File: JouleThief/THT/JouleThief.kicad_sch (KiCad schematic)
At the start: 14 parts, among them J1 Screw_Terminal_01x02, J2 Screw_Terminal_01x02, Q1 BC547, Q2 BC547

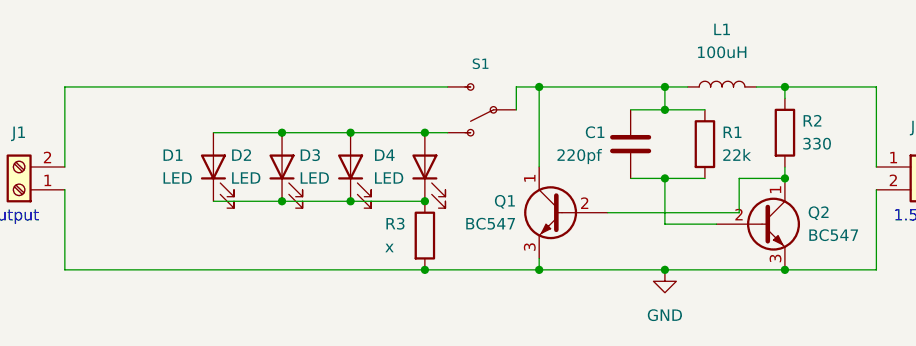
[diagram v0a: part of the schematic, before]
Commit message: Updated Joule thief schematic values
Inductor: 220uH
Capacitor: 100pF
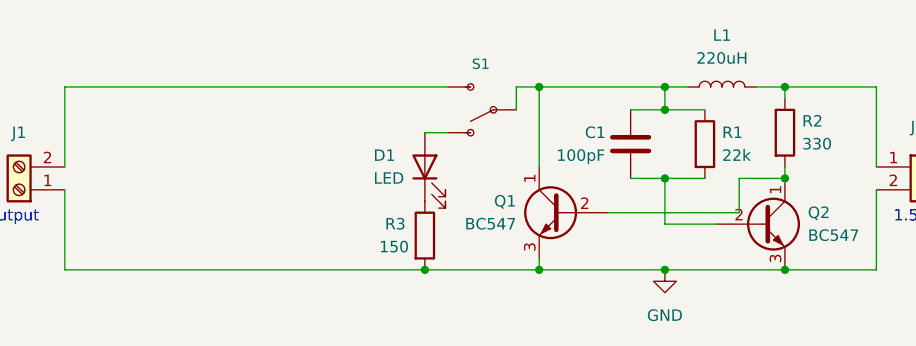
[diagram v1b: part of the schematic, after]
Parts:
- removed D1, D2, D3: LED, LED_SMD:LED_0805_2012Metric_Pad1.15x1.40mm_HandSolder, symbol Device:LED
- C1: value 220pf -> 100pF
- L1: value 100uH -> 220uH
- R3: value x -> 150
- renumbered D4 to D1
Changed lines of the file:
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@@
   (junction (at 151.765 90.805) (diameter 0) (color 0 0 0 0)
   )
-  (junction (at 109.22 95.885) (diameter 0) (color 0 0 0 0)
-  )
   (junction (at 137.795 90.805) (diameter 0) (color 0 0 0 0)
   )
   (junction (at 151.765 100.965) (diameter 0) (color 0 0 0 0)
   )
-  (junction (at 109.22 103.505) (diameter 0) (color 0 0 0 0)
-  )
   (junction (at 165.1 100.965) (diameter 0) (color 0 0 0 0)
   )
-  (junction (at 116.84 103.505) (diameter 0) (color 0 0 0 0)
-  )
   (junction (at 151.765 111.125) (diameter 0) (color 0 0 0 0)
   )
-  (junction (at 125.095 95.885) (diameter 0) (color 0 0 0 0)
-  )
-  (junction (at 116.84 95.885) (diameter 0) (color 0 0 0 0)
-  )
   (junction (at 125.095 111.125) (diameter 0) (color 0 0 0 0)
   )
@@
   (junction (at 165.1 111.125) (diameter 0) (color 0 0 0 0)
   )
-  (junction (at 125.095 103.505) (diameter 0) (color 0 0 0 0)
-  )
   (junction (at 165.1 90.805) (diameter 0) (color 0 0 0 0)
   )
@@
     (stroke (width 0) (type default) (color 0 0 0 0))
   )
-  (wire (pts (xy 109.22 103.505) (xy 116.84 103.505))
-    (stroke (width 0) (type default) (color 0 0 0 0))
-  )
   (wire (pts (xy 137.795 109.855) (xy 137.795 111.125))
     (stroke (width 0) (type default) (color 0 0 0 0))
   )
-  (wire (pts (xy 116.84 103.505) (xy 125.095 103.505))
-    (stroke (width 0) (type default) (color 0 0 0 0))
-  )
   (wire (pts (xy 147.955 100.965) (xy 151.765 100.965))
     (stroke (width 0) (type default) (color 0 0 0 0))
@@
     (stroke (width 0) (type default) (color 0 0 0 0))
   )
-  (wire (pts (xy 116.84 95.885) (xy 125.095 95.885))
-    (stroke (width 0) (type default) (color 0 0 0 0))
-  )
   (wire (pts (xy 156.21 93.345) (xy 151.765 93.345))
     (stroke (width 0) (type default) (color 0 0 0 0))
@@
     (stroke (width 0) (type default) (color 0 0 0 0))
   )
-  (wire (pts (xy 101.6 103.505) (xy 109.22 103.505))
-    (stroke (width 0) (type default) (color 0 0 0 0))
-  )
   (wire (pts (xy 151.765 100.965) (xy 156.21 100.965))
     (stroke (width 0) (type default) (color 0 0 0 0))
@@
     (stroke (width 0) (type default) (color 0 0 0 0))
   )
-  (wire (pts (xy 101.6 95.885) (xy 109.22 95.885))
-    (stroke (width 0) (type default) (color 0 0 0 0))
-  )
   (wire (pts (xy 175.26 90.805) (xy 165.1 90.805))
     (stroke (width 0) (type default) (color 0 0 0 0))
@@
   )
   (wire (pts (xy 135.255 93.345) (xy 135.255 90.805))
-    (stroke (width 0) (type default) (color 0 0 0 0))
-  )
-  (wire (pts (xy 109.22 95.885) (xy 116.84 95.885))
     (stroke (width 0) (type default) (color 0 0 0 0))
   )
@@
     (pin "2")
   )
-  (symbol (lib_id "Device:LED") (at 116.84 99.695 90) (unit 1)
-    (in_bom yes) (on_board yes)
-    (property "Reference" "D3" (id 0) (at 111.125 98.425 90)
-      (effects (font (size 1.27 1.27)) (justify right))
-    )
-    (property "Value" "LED" (id 1) (at 111.125 100.965 90)
-      (effects (font (size 1.27 1.27)) (justify right))
-    )
-    (property "Footprint" "LED_SMD:LED_0805_2012Metric_Pad1.15x1.40mm_HandSolder" (id 2) (at 116.84 99.695 0)
-      (effects (font (size 1.27 1.27)) hide)
-    )
-    (property "Datasheet" "~" (id 3) (at 116.84 99.695 0)
-      (effects (font (size 1.27 1.27)) hide)
-    )
-    (pin "1")
-    (pin "2")
-  )
   (symbol (lib_id "Device:L") (at 158.115 90.805 90) (unit 1)
     (in_bom yes) (on_board yes) (fields_autoplaced)
-    (property "Reference" "L1" (id 0) (at 158.115 84.455 90))
-    (property "Value" "100uH" (id 1) (at 158.115 86.995 90))
+    (property "Reference" "L1" (id 0) (at 158.115 85.09 90))
+    (property "Value" "220uH" (id 1) (at 158.115 87.63 90))
     (property "Footprint" "Inductor_SMD:L_6.3x6.3_H3" (id 2) (at 158.115 90.805 0)
       (effects (font (size 1.27 1.27)) hide)
@@
       (effects (font (size 1.27 1.27)) (justify left))
     )
-    (property "Value" "220pf" (id 1) (at 139.7 98.425 0)
+    (property "Value" "100pF" (id 1) (at 139.7 98.425 0)
       (effects (font (size 1.27 1.27)) (justify left))
     )
@@
     (pin "1")
   )
-  (symbol (lib_id "Device:LED") (at 101.6 99.695 90) (unit 1)
-    (in_bom yes) (on_board yes)
-    (property "Reference" "D1" (id 0) (at 95.885 98.425 90)
-      (effects (font (size 1.27 1.27)) (justify right))
-    )
-    (property "Value" "LED" (id 1) (at 95.885 100.965 90)
-      (effects (font (size 1.27 1.27)) (justify right))
-    )
-    (property "Footprint" "LED_SMD:LED_0805_2012Metric_Pad1.15x1.40mm_HandSolder" (id 2) (at 101.6 99.695 0)
-      (effects (font (size 1.27 1.27)) hide)
-    )
-    (property "Datasheet" "~" (id 3) (at 101.6 99.695 0)
-      (effects (font (size 1.27 1.27)) hide)
-    )
-    (pin "1")
-    (pin "2")
-  )
   (symbol (lib_id "Connector:Screw_Terminal_01x02") (at 80.01 102.235 180) (unit 1)
     (in_bom yes) (on_board yes) (fields_autoplaced)
@@
     (pin "2")
   )
-  (symbol (lib_id "Device:LED") (at 109.22 99.695 90) (unit 1)
-    (in_bom yes) (on_board yes)
-    (property "Reference" "D2" (id 0) (at 103.505 98.425 90)
-      (effects (font (size 1.27 1.27)) (justify right))
-    )
-    (property "Value" "LED" (id 1) (at 103.505 100.965 90)
-      (effects (font (size 1.27 1.27)) (justify right))
-    )
-    (property "Footprint" "LED_SMD:LED_0805_2012Metric_Pad1.15x1.40mm_HandSolder" (id 2) (at 109.22 99.695 0)
-      (effects (font (size 1.27 1.27)) hide)
-    )
-    (property "Datasheet" "~" (id 3) (at 109.22 99.695 0)
-      (effects (font (size 1.27 1.27)) hide)
-    )
-    (pin "1")
-    (pin "2")
-  )
   (symbol (lib_id "Device:R") (at 156.21 97.155 0) (unit 1)
     (in_bom yes) (on_board yes)
@@
   (symbol (lib_id "Device:LED") (at 125.095 99.695 90) (unit 1)
     (in_bom yes) (on_board yes)
-    (property "Reference" "D4" (id 0) (at 119.38 98.425 90)
+    (property "Reference" "D1" (id 0) (at 119.38 98.425 90)
       (effects (font (size 1.27 1.27)) (justify right))
     )
@@
       (effects (font (size 1.27 1.27)) (justify left))
     )
-    (property "Value" "x" (id 1) (at 120.65 108.585 0)
+    (property "Value" "150" (id 1) (at 120.015 108.585 0)
       (effects (font (size 1.27 1.27)) (justify left))
     )
@@
     )
     (path "/56f57a0c-d952-4b14-b499-4833f5f6a321"
-      (reference "C1") (unit 1) (value "220pf") (footprint "Capacitor_SMD:C_0805_2012Metric_Pad1.18x1.45mm_HandSolder")
-    )
-    (path "/a3379bb9-2fa5-4298-a436-0e0faa7bcb5e"
+      (reference "C1") (unit 1) (value "100pF") (footprint "Capacitor_SMD:C_0805_2012Metric_Pad1.18x1.45mm_HandSolder")
+    )
+    (path "/e027e40e-245b-4b6b-928b-0501a7da5de5"
       (reference "D1") (unit 1) (value "LED") (footprint "LED_SMD:LED_0805_2012Metric_Pad1.15x1.40mm_HandSolder")
-    )
-    (path "/d156950b-aa7e-4415-90f6-d17a4996de0e"
-      (reference "D2") (unit 1) (value "LED") (footprint "LED_SMD:LED_0805_2012Metric_Pad1.15x1.40mm_HandSolder")
-    )
-    (path "/2c5e3b91-00a4-441c-a5d0-5cef8c01ab08"
-      (reference "D3") (unit 1) (value "LED") (footprint "LED_SMD:LED_0805_2012Metric_Pad1.15x1.40mm_HandSolder")
-    )
-    (path "/e027e40e-245b-4b6b-928b-0501a7da5de5"
-      (reference "D4") (unit 1) (value "LED") (footprint "LED_SMD:LED_0805_2012Metric_Pad1.15x1.40mm_HandSolder")
     )
     (path "/c5208d8c-5be5-4514-b93e-909a9ac14ee6"
@@
     )
     (path "/41c982a7-98bb-4b69-93c8-cae707855073"
-      (reference "L1") (unit 1) (value "100uH") (footprint "Inductor_SMD:L_6.3x6.3_H3")
+      (reference "L1") (unit 1) (value "220uH") (footprint "Inductor_SMD:L_6.3x6.3_H3")
     )
     (path "/473a4415-2386-4149-a3fe-7889d826e6e0"
@@
     )
     (path "/fec27d13-0747-41e3-a4d8-e21a45052ada"
-      (reference "R3") (unit 1) (value "x") (footprint "Resistor_SMD:R_0805_2012Metric_Pad1.20x1.40mm_HandSolder")
+      (reference "R3") (unit 1) (value "150") (footprint "Resistor_SMD:R_0805_2012Metric_Pad1.20x1.40mm_HandSolder")
     )
     (path "/5a60103d-c1f5-44fb-9ca6-bd09329bef56"

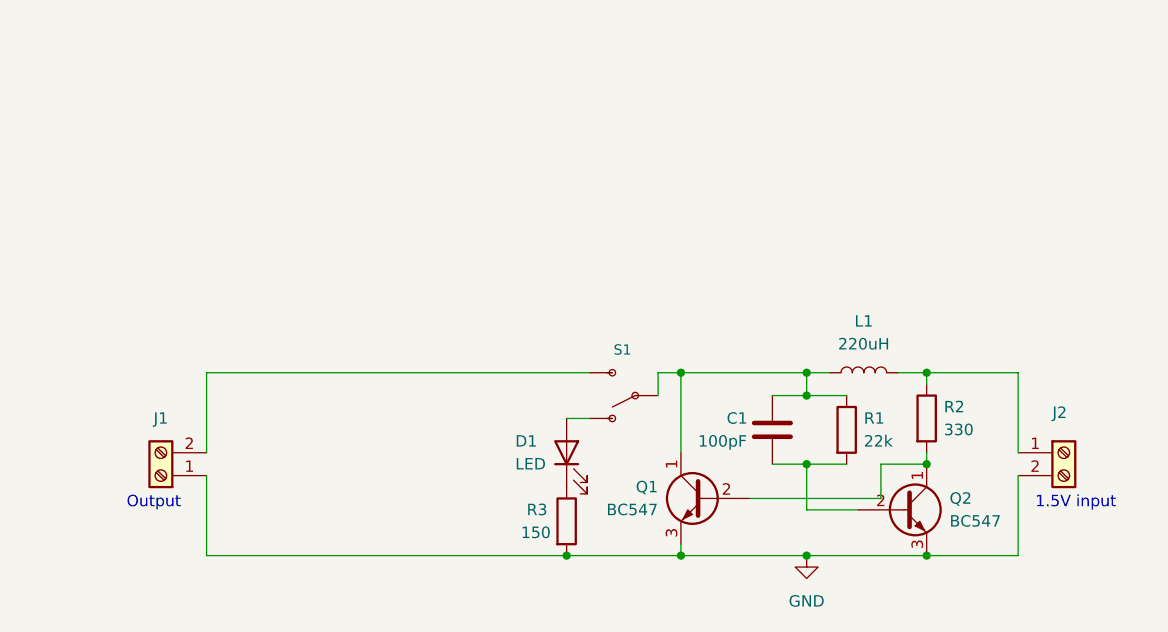
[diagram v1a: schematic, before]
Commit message: added tht components back tot tht
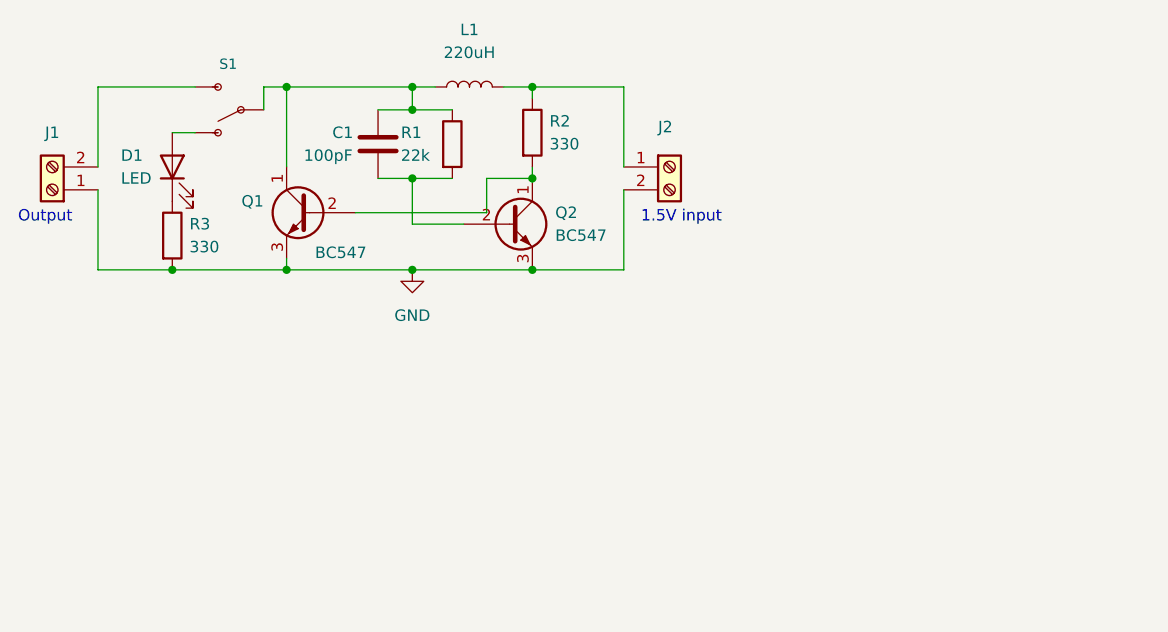
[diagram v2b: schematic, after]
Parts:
- C1: footprint Capacitor_SMD:C_0805_2012Metric_Pad1.18x1.45mm_HandSolder -> Capacitor_THT:C_Axial_L5.1mm_D3.1mm_P7.50mm_Horizontal
- D1: footprint LED_SMD:LED_0805_2012Metric_Pad1.15x1.40mm_HandSolder -> LED_THT:LED_D5.0mm_Clear
- L1: footprint Inductor_SMD:L_6.3x6.3_H3 -> Inductor_THT:L_Axial_L5.0mm_D3.6mm_P10.00mm_Horizontal_Murata_BL01RN1A2A2
- Q1, Q2: footprint SamacSys_Parts:BC847215 -> Package_TO_SOT_THT:TO-92_Inline
- R1, R2: footprint Resistor_SMD:R_0805_2012Metric_Pad1.20x1.40mm_HandSolder -> Resistor_THT:R_Axial_DIN0204_L3.6mm_D1.6mm_P7.62mm_Horizontal
- R3: value 150 -> 330; footprint Resistor_SMD:R_0805_2012Metric_Pad1.20x1.40mm_HandSolder -> Resistor_THT:R_Axial_DIN0204_L3.6mm_D1.6mm_P7.62mm_Horizontal; Purpose led current resistor -> (none)
- S1: footprint SamacSys_Parts:LSSM12PVTR -> SnapEDA Library:SW_1825159-1

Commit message: enh
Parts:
- C1: footprint Capacitor_THT:C_Axial_L5.1mm_D3.1mm_P7.50mm_Horizontal -> Capacitor_SMD:C_0805_2012Metric_Pad1.18x1.45mm_HandSolder
- D1: footprint LED_THT:LED_D5.0mm_Clear -> LED_SMD:LED_0805_2012Metric_Pad1.15x1.40mm_HandSolder
- L1: footprint Inductor_THT:L_Axial_L5.0mm_D3.6mm_P10.00mm_Horizontal_Murata_BL01RN1A2A2 -> Inductor_SMD:L_6.3x6.3_H3
- Q1, Q2: footprint Package_TO_SOT_THT:TO-92_Inline -> SamacSys_Parts:BC847215
- R1, R2, R3: footprint Resistor_THT:R_Axial_DIN0204_L3.6mm_D1.6mm_P7.62mm_Horizontal -> Resistor_SMD:R_0805_2012Metric_Pad1.20x1.40mm_HandSolder
- S1: footprint SnapEDA Library:SW_1825159-1 -> SamacSys_Parts:LSSM12PVTR
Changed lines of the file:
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@@
       (effects (font (size 1.27 1.27)) (justify left))
     )
-    (property "Footprint" "Capacitor_THT:C_Axial_L5.1mm_D3.1mm_P7.50mm_Horizontal" (id 2) (at 105.1052 69.215 0)
+    (property "Footprint" "Capacitor_SMD:C_0805_2012Metric_Pad1.18x1.45mm_HandSolder" (id 2) (at 105.1052 69.215 0)
       (effects (font (size 1.27 1.27)) hide)
     )
@@
     (property "Reference" "L1" (id 0) (at 114.3 52.705 90))
     (property "Value" "220uH" (id 1) (at 114.3 55.245 90))
-    (property "Footprint" "Inductor_THT:L_Axial_L5.0mm_D3.6mm_P10.00mm_Horizontal_Murata_BL01RN1A2A2" (id 2) (at 114.3 59.055 0)
+    (property "Footprint" "Inductor_SMD:L_6.3x6.3_H3" (id 2) (at 114.3 59.055 0)
       (effects (font (size 1.27 1.27)) hide)
     )
@@
       (effects (font (size 1.27 1.27)) (justify left))
     )
-    (property "Footprint" "Package_TO_SOT_THT:TO-92_Inline" (id 2) (at 123.825 76.2 0)
+    (property "Footprint" "SamacSys_Parts:BC847215" (id 2) (at 123.825 76.2 0)
       (effects (font (size 1.27 1.27) italic) (justify left) hide)
     )
@@
       (effects (font (size 1.27 1.27)) (justify left))
     )
-    (property "Footprint" "Resistor_THT:R_Axial_DIN0204_L3.6mm_D1.6mm_P7.62mm_Horizontal" (id 2) (at 110.617 65.405 90)
+    (property "Footprint" "Resistor_SMD:R_0805_2012Metric_Pad1.20x1.40mm_HandSolder" (id 2) (at 110.617 65.405 90)
       (effects (font (size 1.27 1.27)) hide)
     )
@@
       (effects (font (size 1.27 1.27)) (justify left))
     )
-    (property "Footprint" "Resistor_THT:R_Axial_DIN0204_L3.6mm_D1.6mm_P7.62mm_Horizontal" (id 2) (at 119.507 64.135 90)
+    (property "Footprint" "Resistor_SMD:R_0805_2012Metric_Pad1.20x1.40mm_HandSolder" (id 2) (at 119.507 64.135 90)
       (effects (font (size 1.27 1.27)) hide)
     )
@@
       (effects (font (size 1.27 1.27)) (justify right))
     )
-    (property "Footprint" "LED_THT:LED_D5.0mm_Clear" (id 2) (at 81.28 67.945 0)
+    (property "Footprint" "LED_SMD:LED_0805_2012Metric_Pad1.15x1.40mm_HandSolder" (id 2) (at 81.28 67.945 0)
       (effects (font (size 1.27 1.27)) hide)
     )
@@
       (effects (font (size 1.27 1.27)) (justify left))
     )
-    (property "Footprint" "Resistor_THT:R_Axial_DIN0204_L3.6mm_D1.6mm_P7.62mm_Horizontal" (id 2) (at 79.502 75.565 90)
+    (property "Footprint" "Resistor_SMD:R_0805_2012Metric_Pad1.20x1.40mm_HandSolder" (id 2) (at 79.502 75.565 90)
       (effects (font (size 1.27 1.27)) hide)
     )
@@
       (effects (font (size 1.143 1.143)) hide)
     )
-    (property "Footprint" "SnapEDA Library:SW_1825159-1" (id 2) (at 88.9 67.945 0)
+    (property "Footprint" "SamacSys_Parts:LSSM12PVTR" (id 2) (at 88.9 67.945 0)
       (effects (font (size 0.508 0.508)) hide)
     )
@@
       (effects (font (size 1.27 1.27)) (justify left))
     )
-    (property "Footprint" "Package_TO_SOT_THT:TO-92_Inline" (id 2) (at 91.44 74.93 0)
+    (property "Footprint" "SamacSys_Parts:BC847215" (id 2) (at 91.44 74.93 0)
       (effects (font (size 1.27 1.27) italic) (justify left) hide)
     )
@@
     )
     (path "/165ce1d9-ec6c-402f-b137-29c897fe33e9"
-      (reference "C1") (unit 1) (value "100pF") (footprint "Capacitor_THT:C_Axial_L5.1mm_D3.1mm_P7.50mm_Horizontal")
+      (reference "C1") (unit 1) (value "100pF") (footprint "Capacitor_SMD:C_0805_2012Metric_Pad1.18x1.45mm_HandSolder")
     )
     (path "/7e6f3694-d55b-4625-b9f4-5a2ce49e4fea"
-      (reference "D1") (unit 1) (value "LED") (footprint "LED_THT:LED_D5.0mm_Clear")
+      (reference "D1") (unit 1) (value "LED") (footprint "LED_SMD:LED_0805_2012Metric_Pad1.15x1.40mm_HandSolder")
     )
     (path "/2987da22-2eec-4ed1-b4c8-42061a16b495"
@@
     )
     (path "/3d2a249b-2f29-4cd7-a76b-1d51a3ee2fab"
-      (reference "L1") (unit 1) (value "220uH") (footprint "Inductor_THT:L_Axial_L5.0mm_D3.6mm_P10.00mm_Horizontal_Murata_BL01RN1A2A2")
+      (reference "L1") (unit 1) (value "220uH") (footprint "Inductor_SMD:L_6.3x6.3_H3")
     )
     (path "/fbe24f0e-fbe5-41ce-aecf-066aa14fabc3"
-      (reference "Q1") (unit 1) (value "BC547") (footprint "Package_TO_SOT_THT:TO-92_Inline")
+      (reference "Q1") (unit 1) (value "BC547") (footprint "SamacSys_Parts:BC847215")
     )
     (path "/56f97ceb-2f89-45b9-8233-472a8c58f4ba"
-      (reference "Q2") (unit 1) (value "BC547") (footprint "Package_TO_SOT_THT:TO-92_Inline")
+      (reference "Q2") (unit 1) (value "BC547") (footprint "SamacSys_Parts:BC847215")
     )
     (path "/599fa2b0-cb4d-4f48-a63f-0382fedb8334"
-      (reference "R1") (unit 1) (value "22k") (footprint "Resistor_THT:R_Axial_DIN0204_L3.6mm_D1.6mm_P7.62mm_Horizontal")
+      (reference "R1") (unit 1) (value "22k") (footprint "Resistor_SMD:R_0805_2012Metric_Pad1.20x1.40mm_HandSolder")
     )
     (path "/5b4da779-33b4-456c-8ed4-c656d4dde8be"
-      (reference "R2") (unit 1) (value "330") (footprint "Resistor_THT:R_Axial_DIN0204_L3.6mm_D1.6mm_P7.62mm_Horizontal")
+      (reference "R2") (unit 1) (value "330") (footprint "Resistor_SMD:R_0805_2012Metric_Pad1.20x1.40mm_HandSolder")
     )
     (path "/9d64a416-99e7-4e05-b7be-bdba073d7f38"
-      (reference "R3") (unit 1) (value "330") (footprint "Resistor_THT:R_Axial_DIN0204_L3.6mm_D1.6mm_P7.62mm_Horizontal")
+      (reference "R3") (unit 1) (value "330") (footprint "Resistor_SMD:R_0805_2012Metric_Pad1.20x1.40mm_HandSolder")
     )
     (path "/b7f5716e-14a0-4646-be2e-7ae2697fc9f1"
-      (reference "S1") (unit 1) (value "SWITCH-SPDT-PTH-11.6X4.0MM-KIT") (footprint "SnapEDA Library:SW_1825159-1")
-    )
-  )
+      (reference "S1") (unit 1) (value "SWITCH-SPDT-PTH-11.6X4.0MM-KIT") (footprint "SamacSys_Parts:LSSM12PVTR")
+    )
+  )
